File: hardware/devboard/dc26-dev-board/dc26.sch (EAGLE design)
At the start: 112 parts, among them CN1 JST, IC3 LDL112D33R, J1 DC26 Shitty AddOn, J2 DC26 Shitty AddOn, P1 SSSS811101, Y1 ABL-8.000MHZ-B2

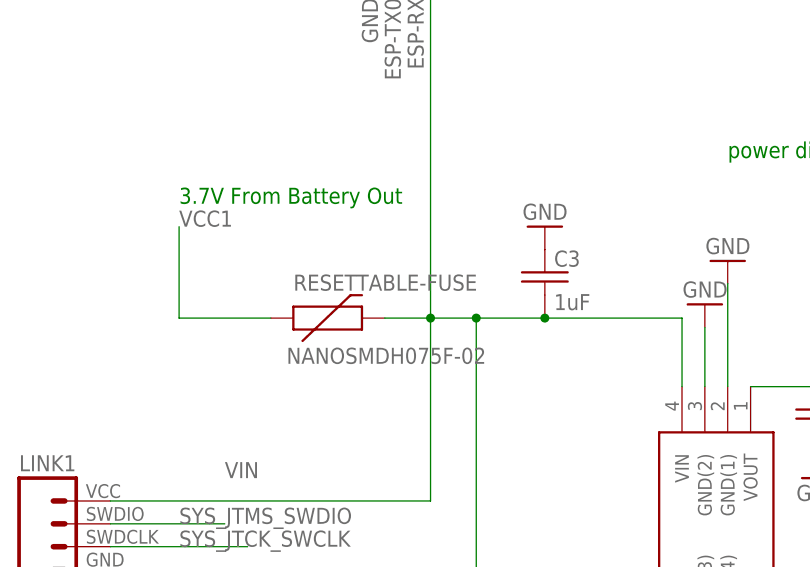
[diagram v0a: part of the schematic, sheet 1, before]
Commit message: clean up of silk screen and artwork
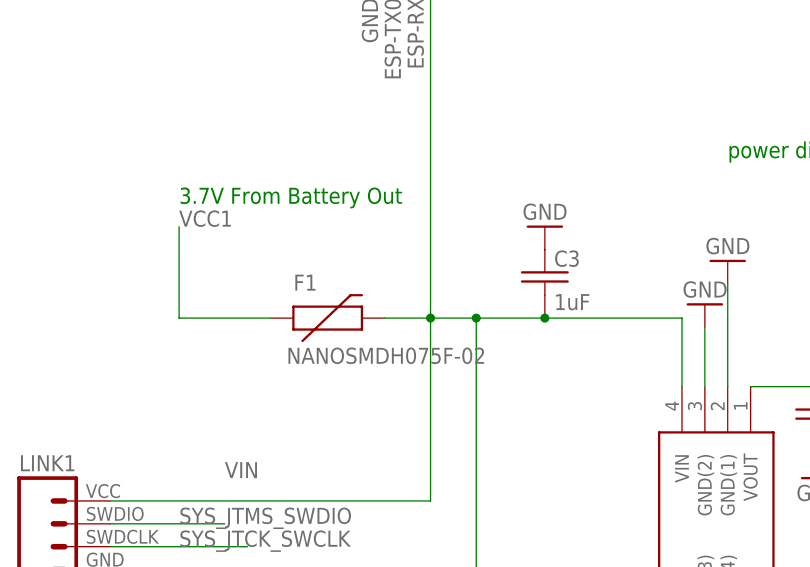
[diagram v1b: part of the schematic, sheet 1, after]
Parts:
- renumbered RESETTABLE-FUSE to F1
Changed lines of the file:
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@@
 <?xml version="1.0" encoding="utf-8"?>
 <!DOCTYPE eagle SYSTEM "eagle.dtd">
-<eagle version="8.7.1">
+<eagle version="7.7.0">
 <drawing>
 <settings>
 <setting alwaysvectorfont="no"/>
-<setting keepoldvectorfont="yes"/>
 <setting verticaltext="up"/>
 </settings>
@@
 <part name="LINK1" library="dc-26" deviceset="STLINK-V2-CONNECTOR" device=""/>
 <part name="GND5" library="dc-26" deviceset="GND" device=""/>
-<part name="RESETTABLE-FUSE" library="dc-26" deviceset="PTC" device="SMD" value="NANOSMDH075F-02"/>
+<part name="F1" library="dc-26" deviceset="PTC" device="SMD" value="NANOSMDH075F-02"/>
 <part name="P1" library="dc-26" deviceset="SWITCH_SPDT" device="" value="SSSS811101"/>
 <part name="R2" library="dc-26" deviceset="RESISTOR" device="0805-RES" value="470"/>
@@
 <instance part="R2" gate="G$1" x="-7.62" y="81.28" rot="R90"/>
 <instance part="R3" gate="G$1" x="27.94" y="71.12" rot="R90"/>
-<instance part="RESETTABLE-FUSE" gate="G$1" x="127" y="96.52"/>
+<instance part="F1" gate="G$1" x="127" y="96.52"/>
 <instance part="P1" gate="G$1" x="157.48" y="50.8"/>
 <instance part="C3" gate="G$1" x="152.4" y="101.6"/>
@@
 </segment>
 <segment>
-<pinref part="RESETTABLE-FUSE" gate="G$1" pin="1"/>
+<pinref part="F1" gate="G$1" pin="1"/>
 <wire x1="111.76" y1="106.68" x2="111.76" y2="96.52" width="0.1524" layer="91"/>
 <wire x1="111.76" y1="96.52" x2="121.92" y2="96.52" width="0.1524" layer="91"/>
@@
 <wire x1="139.7" y1="76.2" x2="139.7" y2="96.52" width="0.1524" layer="91"/>
 <pinref part="C3" gate="G$1" pin="2"/>
-<pinref part="RESETTABLE-FUSE" gate="G$1" pin="2"/>
+<pinref part="F1" gate="G$1" pin="2"/>
 <wire x1="152.4" y1="96.52" x2="144.78" y2="96.52" width="0.1524" layer="91"/>
 <junction x="152.4" y="96.52"/>

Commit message: adding real data sheet for switch
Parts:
- P1: value SSSS811101 -> SPDT_SSAJ120100
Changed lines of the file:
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@@
 <?xml version="1.0" encoding="utf-8"?>
 <!DOCTYPE eagle SYSTEM "eagle.dtd">
-<eagle version="7.7.0">
+<eagle version="9.0.1">
 <drawing>
 <settings>
 <setting alwaysvectorfont="no"/>
+<setting keepoldvectorfont="yes"/>
 <setting verticaltext="up"/>
 </settings>
@@
 <part name="GND5" library="dc-26" deviceset="GND" device=""/>
 <part name="F1" library="dc-26" deviceset="PTC" device="SMD" value="NANOSMDH075F-02"/>
-<part name="P1" library="dc-26" deviceset="SWITCH_SPDT" device="" value="SSSS811101"/>
+<part name="P1" library="dc-26" deviceset="SWITCH_SPDT" device="" value="SPDT_SSAJ120100"/>
 <part name="R2" library="dc-26" deviceset="RESISTOR" device="0805-RES" value="470"/>
 <part name="R3" library="dc-26" deviceset="RESISTOR" device="0805-RES" value="2k"/>
